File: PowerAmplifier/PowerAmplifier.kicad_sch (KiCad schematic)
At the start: 99 parts, among them J1 A_SE, J10 AMP, J11 OSC, J12 12V, J2 AB_IN, J3 AB_BTL, J4 B_SE, J5 C_SE, J6 CD_IN, J7 CD_BTL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

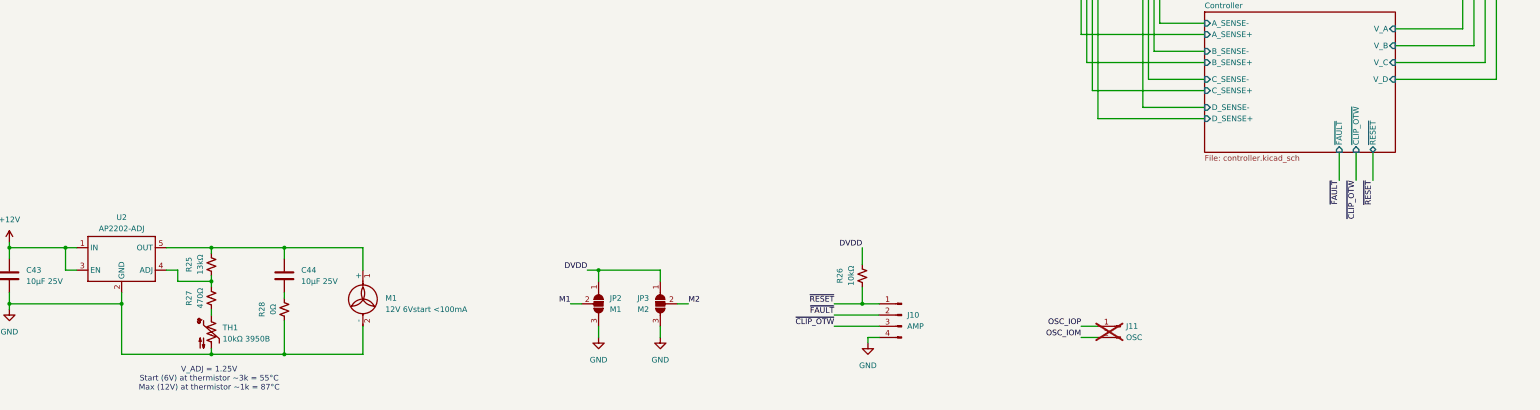
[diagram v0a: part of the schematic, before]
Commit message: PowerAmplifier initially complete, PowerAmpSupply progress
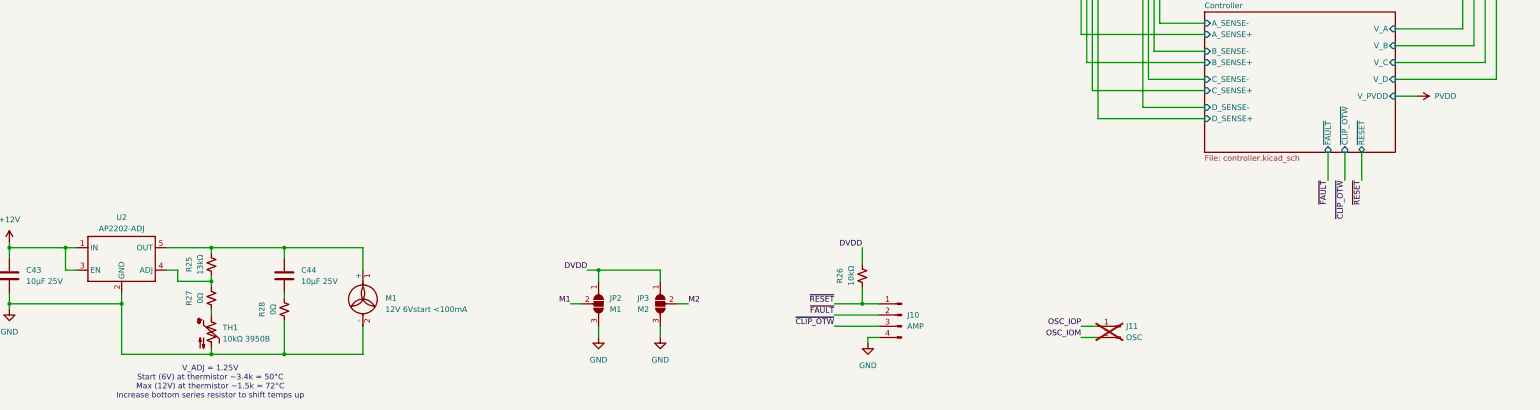
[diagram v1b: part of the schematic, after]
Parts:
- R27: value 470Ω -> 0Ω
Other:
- sheet Controller ports: added V_PVDD; removed none
- note added: "V_ADJ = 1.25V Start (6V) at thermistor ~3.4k = 50°C Max (12V) at thermistor ~1.5k = 72°C Increase bottom series resistor to shift temps up"
- note removed: "V_ADJ = 1.25V Start (6V) at thermistor ~3k = 55°C Max (12V) at thermistor ~1k = 87°C"
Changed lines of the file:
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@@
 	(wire
 		(pts
+			(xy 439.42 287.02) (xy 444.5 287.02)
+		)
+		(stroke
+			(width 0)
+			(type default)
+		)
+	)
+	(wire
+		(pts
 			(xy 337.82 173.99) (xy 336.55 173.99)
 		)
@@
 	(wire
 		(pts
-			(xy 430.53 299.72) (xy 430.53 306.07)
+			(xy 427.99 299.72) (xy 427.99 306.07)
 		)
 		(stroke
@@
 	(wire
 		(pts
-			(xy 426.72 299.72) (xy 426.72 306.07)
+			(xy 424.18 299.72) (xy 424.18 306.07)
 		)
 		(stroke
@@
 	(wire
 		(pts
-			(xy 434.34 299.72) (xy 434.34 306.07)
+			(xy 431.8 299.72) (xy 431.8 306.07)
 		)
 		(stroke
@@
 		)
 	)
-	(text "V_ADJ = 1.25V\nStart (6V) at thermistor ~3k = 55°C\nMax (12V) at thermistor ~1k = 87°C"
+	(text "V_ADJ = 1.25V\nStart (6V) at thermistor ~3.4k = 50°C\nMax (12V) at thermistor ~1.5k = 72°C\nIncrease bottom series resistor to shift temps up"
 		(exclude_from_sim no)
-		(at 170.942 351.028 0)
+		(at 171.196 351.79 0)
 		(effects
 			(font
@@
 	)
 	(label "~{CLIP_OTW}"
-		(at 430.53 306.07 270)
+		(at 427.99 306.07 270)
 		(fields_autoplaced yes)
 		(effects
@@
 	)
 	(label "~{RESET}"
-		(at 434.34 306.07 270)
+		(at 431.8 306.07 270)
 		(fields_autoplaced yes)
 		(effects
@@
 	)
 	(label "~{FAULT}"
-		(at 426.72 306.07 270)
+		(at 424.18 306.07 270)
 		(fields_autoplaced yes)
 		(effects
@@
 	)
 	(symbol
+		(lib_id "power:VDD")
+		(at 444.5 287.02 270)
+		(unit 1)
+		(exclude_from_sim no)
+		(in_bom yes)
+		(on_board yes)
+		(dnp no)
+		(fields_autoplaced yes)
+		(property "Reference" "#PWR056"
+			(at 440.69 287.02 0)
+			(effects
+				(font
+					(size 1.27 1.27)
+				)
+				(hide yes)
+			)
+		)
+		(property "Value" "PVDD"
+			(at 448.31 287.0199 90)
+			(effects
+				(font
+					(size 1.27 1.27)
+				)
+				(justify left)
+			)
+		)
+		(property "Footprint" ""
+			(at 444.5 287.02 0)
+			(effects
+				(font
+					(size 1.27 1.27)
+				)
+				(hide yes)
+			)
+		)
+		(property "Datasheet" ""
+			(at 444.5 287.02 0)
+			(effects
+				(font
+					(size 1.27 1.27)
+				)
+				(hide yes)
+			)
+		)
+		(property "Description" "Power symbol creates a global label with name \"VDD\""
+			(at 444.5 287.02 0)
+			(effects
+				(font
+					(size 1.27 1.27)
+				)
+				(hide yes)
+			)
+		)
+		(pin "1"
+		)
+		(instances
+			(project "PowerAmplifier"
+				(path "/98e31663-11f4-4a7e-ae88-851a6ca7c9bc"
+					(reference "#PWR056")
+					(unit 1)
+				)
+			)
+		)
+	)
+	(symbol
 		(lib_id "power:GND")
 		(at 217.17 234.95 90)
@@
 			)
 		)
-		(property "Value" "470Ω"
+		(property "Value" "0Ω"
 			(at 168.91 332.74 90)
 			(effects
@@
 		)
 		(pin "~{FAULT}" input
-			(at 426.72 299.72 270)
+			(at 424.18 299.72 270)
 			(effects
 				(font
@@
 		)
 		(pin "~{CLIP_OTW}" input
-			(at 430.53 299.72 270)
+			(at 427.99 299.72 270)
 			(effects
 				(font
@@
 		)
 		(pin "~{RESET}" bidirectional
-			(at 434.34 299.72 270)
+			(at 431.8 299.72 270)
 			(effects
 				(font
@@
 			(effects
 				(font
+					(size 1.27 1.27)
+				)
+				(justify right)
+			)
+		)
+		(pin "V_PVDD" input
+			(at 439.42 287.02 0)
+			(effects
+				(font

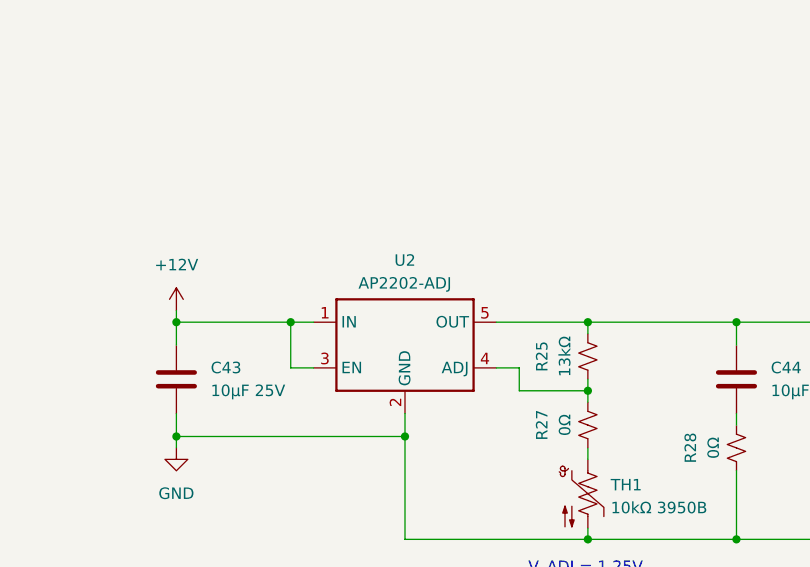
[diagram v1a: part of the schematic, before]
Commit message: PowerAmp+Supply fan LDO change, Supply Rgate fix
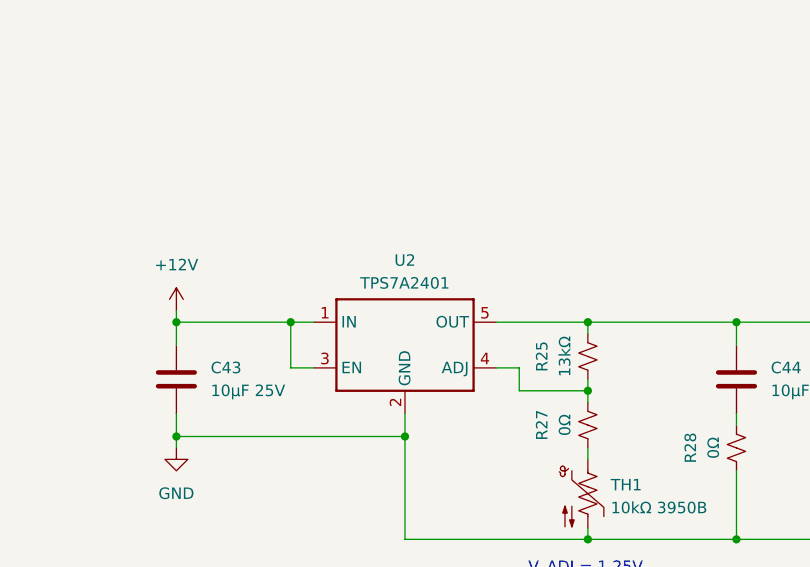
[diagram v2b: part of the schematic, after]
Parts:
- U2: value AP2202-ADJ -> TPS7A2401
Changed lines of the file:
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@@
 			)
 		)
-		(property "Value" "AP2202-ADJ"
+		(property "Value" "TPS7A2401"
 			(at 151.13 316.992 0)
 			(effects

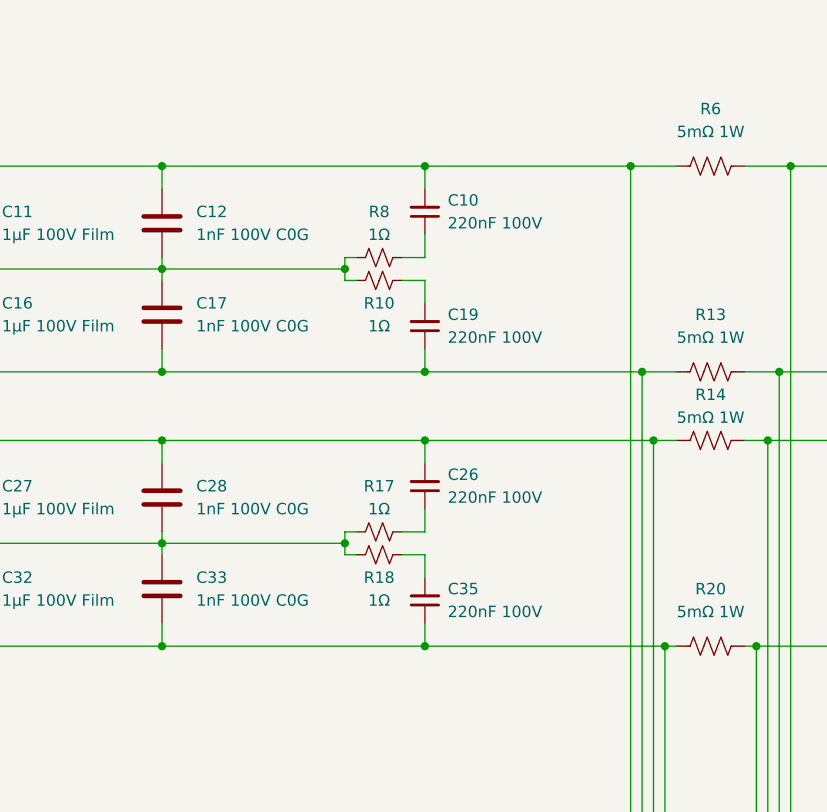
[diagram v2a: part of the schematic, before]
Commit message: PowerAmplifier zobel resistor fix
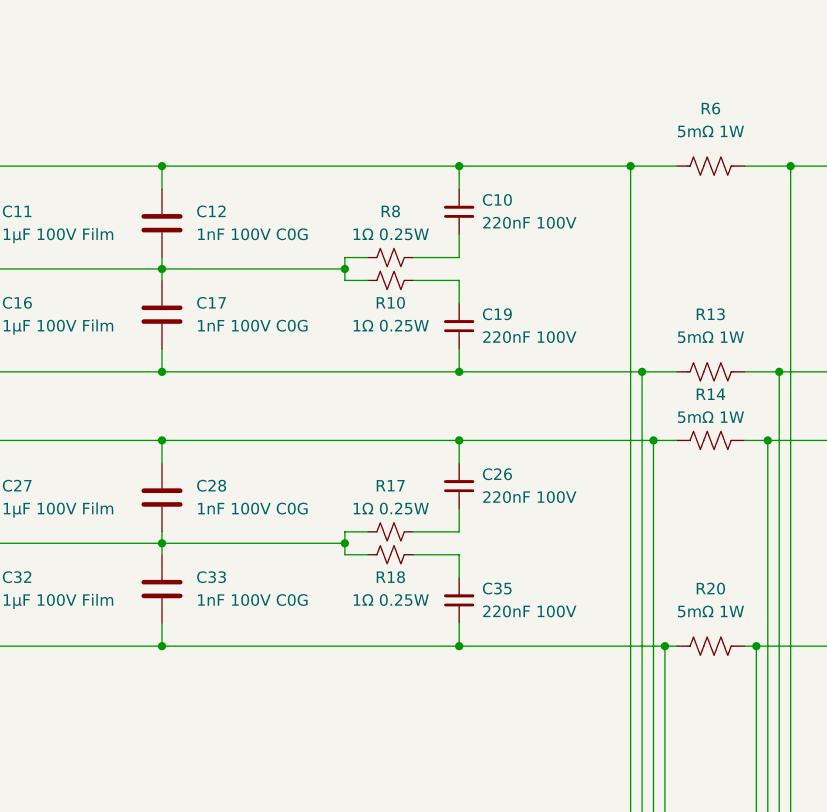
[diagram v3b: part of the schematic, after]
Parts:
- R10, R17, R18, R8: value 1Ω -> 1Ω 0.25W
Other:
- moved on the sheet: C10, C19, C26, C35, R10, R17, R18, R8
